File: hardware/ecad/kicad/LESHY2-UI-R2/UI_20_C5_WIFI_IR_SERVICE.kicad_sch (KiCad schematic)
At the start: 96 parts, among them J6 Samtec FTSH-105-01-L-DV-K-P-TR, J7 GCT RFPC-SMA32-FN-175-A, J8 Hirose U.FL-R-SMT-1(80), J9 GCT USB4105-GF-A, Q2 Diodes Incorporated 2N7002DW-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, Q3 Diodes Incorporated DMN2056U-7, Q4 Diodes Incorporated DMN2056U-7, Q5 Diodes Incorporated DMN2056U-7, SW18 Alps Alpine SKRTLAE010, SW19 Alps Alpine SKRTLAE010, U14 ESP32-C5-WROOM-1U-N8R8, U15 Texas Instruments TPD4E05U06D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, U16 KYOCERA AVX CP0603Q5425ENTR, U17 74LVC2G14GV,125, U18 SN74LVC1G74DCUR, U19 74HC20PW,118, U20 74LVC2G14GV,125, U21 Texas Instruments TPD2EUSB30A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, U22 onsemi FSUSB42MUX, U23 Vishay TSMP95000TT, U24 Vishay TSOP75238TR, U25 Texas Instruments TPS22919DCKR, U26 Nexperia 74LVC2G126DP,125, U27 SN74LVC1G08DCKR

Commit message: Bind H6 RF and USB routing geometry
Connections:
- net C5_SERVICE_USB_DM_BRANCH renamed C5_SERVICE_USB_BRANCH_N
- net C5_SERVICE_USB_DM_CONNECTOR renamed C5_SERVICE_USB_CONNECTOR_N
- net C5_SERVICE_USB_DP_BRANCH renamed C5_SERVICE_USB_BRANCH_P
- net C5_SERVICE_USB_DP_CONNECTOR renamed C5_SERVICE_USB_CONNECTOR_P
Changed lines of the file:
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@@
 		(effects (font (size 1.27 1.27)))
 	)
-	(label "C5_SERVICE_USB_DP_CONNECTOR"
+	(label "C5_SERVICE_USB_CONNECTOR_P"
 		(at 858.52 91.44 0)
 		(effects (font (size 1.27 1.27)))
 	)
-	(label "C5_SERVICE_USB_DM_CONNECTOR"
+	(label "C5_SERVICE_USB_CONNECTOR_N"
 		(at 858.52 93.98 0)
 		(effects (font (size 1.27 1.27)))
@@
 		(effects (font (size 1.27 1.27)) (justify right bottom))
 	)
-	(label "C5_SERVICE_USB_DP_CONNECTOR"
+	(label "C5_SERVICE_USB_CONNECTOR_P"
 		(at 899.16 88.90 180)
 		(effects (font (size 1.27 1.27)) (justify right bottom))
 	)
-	(label "C5_SERVICE_USB_DM_CONNECTOR"
+	(label "C5_SERVICE_USB_CONNECTOR_N"
 		(at 899.16 91.44 180)
 		(effects (font (size 1.27 1.27)) (justify right bottom))
@@
 		)
 	)
-	(label "C5_SERVICE_USB_DM_BRANCH"
+	(label "C5_SERVICE_USB_BRANCH_N"
 		(at 584.20 195.58 0)
 		(effects (font (size 1.27 1.27)))
 	)
-	(label "C5_SERVICE_USB_DM_CONNECTOR"
+	(label "C5_SERVICE_USB_CONNECTOR_N"
 		(at 624.84 195.58 180)
 		(effects (font (size 1.27 1.27)) (justify right bottom))
@@
 		)
 	)
-	(label "C5_SERVICE_USB_DP_BRANCH"
+	(label "C5_SERVICE_USB_BRANCH_P"
 		(at 858.52 205.74 0)
 		(effects (font (size 1.27 1.27)))
 	)
-	(label "C5_SERVICE_USB_DP_CONNECTOR"
+	(label "C5_SERVICE_USB_CONNECTOR_P"
 		(at 899.16 205.74 180)
 		(effects (font (size 1.27 1.27)) (justify right bottom))
@@
 		)
 	)
-	(label "C5_SERVICE_USB_DP_CONNECTOR"
+	(label "C5_SERVICE_USB_CONNECTOR_P"
 		(at 492.76 299.72 0)
 		(effects (font (size 1.27 1.27)))
 	)
-	(label "C5_SERVICE_USB_DM_CONNECTOR"
+	(label "C5_SERVICE_USB_CONNECTOR_N"
 		(at 492.76 302.26 0)
 		(effects (font (size 1.27 1.27)))
@@
 		(effects (font (size 1.27 1.27)))
 	)
-	(label "C5_SERVICE_USB_DM_BRANCH"
+	(label "C5_SERVICE_USB_BRANCH_N"
 		(at 716.28 297.18 180)
 		(effects (font (size 1.27 1.27)) (justify right bottom))
 	)
-	(label "C5_SERVICE_USB_DP_BRANCH"
+	(label "C5_SERVICE_USB_BRANCH_P"
 		(at 716.28 299.72 180)
 		(effects (font (size 1.27 1.27)) (justify right bottom))

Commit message: Canonicalize physical ground anchors
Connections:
- net /UI_10_S3_CORE_MEMORY_BOOT/POWER_GROUND is gone; now on net POWER_GROUND: U14.1 (GND), U14.28 (GND), U14.29 (GND), U14.30 (GND), U14.32 (GND)
- net C5_DBG_ESD_RETURN is gone; now on net POWER_GROUND: U15.3 (GND_3), U15.8 (GND_8)
- net C5_RF_GROUND is gone; now on net POWER_GROUND: J8.2 (SHELL), R94.2 (END_2)
- net C5_SMA_RF_GROUND is gone; now on net POWER_GROUND: J7.2 (GROUND_TOP_LEFT), J7.3 (GROUND_TOP_RIGHT), J7.4 (GROUND_BOTTOM_LEFT), J7.5 (GROUND_BOTTOM_RIGHT)
- net SAFETY_GROUND is gone; now on net POWER_GROUND: C21.2 (END_2), C23.2 (END_2), C24.2 (END_2), C25.2 (END_2), C26.2 (END_2), C27.2 (END_2), C31.2 (END_2), C32.2 (END_2), C37.2 (END_2), Q2.1 (S2), Q2.4 (S1), Q3.2 (S), Q4.2 (S), R111.2 (END_2), R123.2 (END_2), R125.2 (END_2), R127.2 (END_2), R85.2 (END_2), R87.2 (END_2), R89.2 (END_2), R91.2 (END_2), R92.2 (END_2), U17.2 (GND), U18.1 (CLK), U18.2 (D), U18.4 (GND), U19.7 (GND), U20.2 (GND), U27.3 (GND)
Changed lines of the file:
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@@
 		(effects (font (size 1.27 1.27)))
 	)
-	(hierarchical_label "SAFETY_GROUND"
+	(hierarchical_label "POWER_GROUND"
 		(shape bidirectional)
 		(at 76.20 50.80 180)
@@
 		(effects (font (size 1.27 1.27)))
 	)
-	(label "SAFETY_GROUND"
+	(label "POWER_GROUND"
 		(at 259.08 50.80 180)
 		(effects (font (size 1.27 1.27)) (justify right bottom))
@@
 		(effects (font (size 1.27 1.27)))
 	)
-	(label "SAFETY_GROUND"
+	(label "POWER_GROUND"
 		(at 350.52 50.80 180)
 		(effects (font (size 1.27 1.27)) (justify right bottom))
@@
 		(effects (font (size 1.27 1.27)))
 	)
-	(label "SAFETY_GROUND"
+	(label "POWER_GROUND"
 		(at 441.96 50.80 180)
 		(effects (font (size 1.27 1.27)) (justify right bottom))
@@
 		(effects (font (size 1.27 1.27)))
 	)
-	(label "SAFETY_GROUND"
+	(label "POWER_GROUND"
 		(at 533.40 50.80 180)
 		(effects (font (size 1.27 1.27)) (justify right bottom))
@@
 		(effects (font (size 1.27 1.27)))
 	)
-	(label "SAFETY_GROUND"
+	(label "POWER_GROUND"
 		(at 624.84 50.80 180)
 		(effects (font (size 1.27 1.27)) (justify right bottom))
@@
 		(effects (font (size 1.27 1.27)))
 	)
-	(hierarchical_label "POWER_GROUND"
-		(shape bidirectional)
+	(label "POWER_GROUND"
 		(at 716.28 50.80 180)
 		(effects (font (size 1.27 1.27)) (justify right bottom))
@@
 		(effects (font (size 1.27 1.27)))
 	)
-	(label "SAFETY_GROUND"
+	(label "POWER_GROUND"
 		(at 990.60 50.80 180)
 		(effects (font (size 1.27 1.27)) (justify right bottom))
@@
 		(effects (font (size 1.27 1.27)))
 	)
-	(label "SAFETY_GROUND"
+	(label "POWER_GROUND"
 		(at 1082.04 50.80 180)
 		(effects (font (size 1.27 1.27)) (justify right bottom))
@@
 		(effects (font (size 1.27 1.27)))
 	)
-	(label "SAFETY_GROUND"
+	(label "POWER_GROUND"
 		(at 441.96 86.36 180)
 		(effects (font (size 1.27 1.27)) (justify right bottom))
@@
 		(effects (font (size 1.27 1.27)))
 	)
-	(label "C5_SMA_RF_GROUND"
+	(label "POWER_GROUND"
 		(at 675.64 87.63 0)
 		(effects (font (size 1.27 1.27)))
 	)
-	(label "C5_SMA_RF_GROUND"
+	(label "POWER_GROUND"
 		(at 675.64 90.17 0)
 		(effects (font (size 1.27 1.27)))
 	)
-	(label "C5_SMA_RF_GROUND"
+	(label "POWER_GROUND"
 		(at 716.28 85.09 180)
 		(effects (font (size 1.27 1.27)) (justify right bottom))
 	)
-	(label "C5_SMA_RF_GROUND"
+	(label "POWER_GROUND"
 		(at 716.28 87.63 180)
 		(effects (font (size 1.27 1.27)) (justify right bottom))
@@
 		(effects (font (size 1.27 1.27)))
 	)
-	(label "C5_RF_GROUND"
+	(label "POWER_GROUND"
 		(at 807.72 86.36 180)
 		(effects (font (size 1.27 1.27)) (justify right bottom))
@@
 		)
 	)
-	(label "SAFETY_GROUND"
+	(label "POWER_GROUND"
 		(at 949.96 85.09 0)
 		(effects (font (size 1.27 1.27)))
@@
 		(effects (font (size 1.27 1.27)))
 	)
-	(label "SAFETY_GROUND"
+	(label "POWER_GROUND"
 		(at 990.60 85.09 180)
 		(effects (font (size 1.27 1.27)) (justify right bottom))
@@
 		(effects (font (size 1.27 1.27)))
 	)
-	(label "SAFETY_GROUND"
+	(label "POWER_GROUND"
 		(at 1041.40 88.90 0)
 		(effects (font (size 1.27 1.27)))
@@
 		(effects (font (size 1.27 1.27)))
 	)
-	(label "SAFETY_GROUND"
+	(label "POWER_GROUND"
 		(at 35.56 124.46 0)
 		(effects (font (size 1.27 1.27)))
@@
 		(effects (font (size 1.27 1.27)))
 	)
-	(label "SAFETY_GROUND"
+	(label "POWER_GROUND"
 		(at 899.16 134.62 180)
 		(effects (font (size 1.27 1.27)) (justify right bottom))
@@
 		(effects (font (size 1.27 1.27)))
 	)
-	(label "SAFETY_GROUND"
+	(label "POWER_GROUND"
 		(at 167.64 157.48 180)
 		(effects (font (size 1.27 1.27)) (justify right bottom))
@@
 		(effects (font (size 1.27 1.27)))
 	)
-	(label "SAFETY_GROUND"
+	(label "POWER_GROUND"
 		(at 350.52 157.48 180)
 		(effects (font (size 1.27 1.27)) (justify right bottom))
@@
 		(effects (font (size 1.27 1.27)))
 	)
-	(label "SAFETY_GROUND"
+	(label "POWER_GROUND"
 		(at 533.40 157.48 180)
 		(effects (font (size 1.27 1.27)) (justify right bottom))
@@
 		(effects (font (size 1.27 1.27)))
 	)
-	(label "SAFETY_GROUND"
+	(label "POWER_GROUND"
 		(at 716.28 157.48 180)
 		(effects (font (size 1.27 1.27)) (justify right bottom))
@@
 		(effects (font (size 1.27 1.27)))
 	)
-	(label "C5_RF_GROUND"
+	(label "POWER_GROUND"
 		(at 990.60 157.48 180)
 		(effects (font (size 1.27 1.27)) (justify right bottom))
@@
 		(effects (font (size 1.27 1.27)))
 	)
-	(label "SAFETY_GROUND"
+	(label "POWER_GROUND"
 		(at 167.64 228.60 180)
 		(effects (font (size 1.27 1.27)) (justify right bottom))
@@
 		(effects (font (size 1.27 1.27)))
 	)
-	(label "SAFETY_GROUND"
+	(label "POWER_GROUND"
 		(at 167.64 264.16 180)
 		(effects (font (size 1.27 1.27)) (justify right bottom))
@@
 		(effects (font (size 1.27 1.27)))
 	)
-	(label "SAFETY_GROUND"
+	(label "POWER_GROUND"
 		(at 350.52 264.16 180)
 		(effects (font (size 1.27 1.27)) (justify right bottom))
@@
 		(effects (font (size 1.27 1.27)))
 	)
-	(label "SAFETY_GROUND"
+	(label "POWER_GROUND"
 		(at 533.40 264.16 180)
 		(effects (font (size 1.27 1.27)) (justify right bottom))
@@
 		)
 	)
-	(hierarchical_label "/UI_10_S3_CORE_MEMORY_BOOT/POWER_GROUND"
-		(shape bidirectional)
+	(label "POWER_GROUND"
 		(at 584.20 264.16 0)
 		(effects (font (size 1.27 1.27)))
@@
 	(no_connect (at 624.84 289.56)
 	)
-	(label "/UI_10_S3_CORE_MEMORY_BOOT/POWER_GROUND"
+	(label "POWER_GROUND"
 		(at 624.84 292.10 180)
 		(effects (font (size 1.27 1.27)) (justify right bottom))
 	)
-	(label "/UI_10_S3_CORE_MEMORY_BOOT/POWER_GROUND"
+	(label "POWER_GROUND"
 		(at 624.84 294.64 180)
 		(effects (font (size 1.27 1.27)) (justify right bottom))
 	)
-	(label "/UI_10_S3_CORE_MEMORY_BOOT/POWER_GROUND"
+	(label "POWER_GROUND"
 		(at 624.84 297.18 180)
 		(effects (font (size 1.27 1.27)) (justify right bottom))
@@
 	(no_connect (at 624.84 299.72)
 	)
-	(label "/UI_10_S3_CORE_MEMORY_BOOT/POWER_GROUND"
+	(label "POWER_GROUND"
 		(at 624.84 302.26 180)
 		(effects (font (size 1.27 1.27)) (justify right bottom))
@@
 		(effects (font (size 1.27 1.27)))
 	)
-	(label "C5_DBG_ESD_RETURN"
+	(label "POWER_GROUND"
 		(at 858.52 279.40 0)
 		(effects (font (size 1.27 1.27)))
@@
 	(no_connect (at 899.16 276.86)
 	)
-	(label "C5_DBG_ESD_RETURN"
+	(label "POWER_GROUND"
 		(at 899.16 279.40 180)
 		(effects (font (size 1.27 1.27)) (justify right bottom))
@@
 		(effects (font (size 1.27 1.27)))
 	)
-	(label "SAFETY_GROUND"
+	(label "POWER_GROUND"
 		(at 127.00 300.99 0)
 		(effects (font (size 1.27 1.27)))
@@
 		)
 	)
-	(label "SAFETY_GROUND"
+	(label "POWER_GROUND"
 		(at 218.44 297.18 0)
 		(effects (font (size 1.27 1.27)))
 	)
-	(label "SAFETY_GROUND"
+	(label "POWER_GROUND"
 		(at 218.44 299.72 0)
 		(effects (font (size 1.27 1.27)))
@@
 	(no_connect (at 218.44 302.26)
 	)
-	(label "SAFETY_GROUND"
+	(label "POWER_GROUND"
 		(at 218.44 304.80 0)
 		(effects (font (size 1.27 1.27)))
@@
 		(effects (font (size 1.27 1.27)))
 	)
-	(label "SAFETY_GROUND"
+	(label "POWER_GROUND"
 		(at 309.88 312.42 0)
 		(effects (font (size 1.27 1.27)))
@@
 		(effects (font (size 1.27 1.27)))
 	)
-	(label "SAFETY_GROUND"
+	(label "POWER_GROUND"
 		(at 401.32 300.99 0)
 		(effects (font (size 1.27 1.27)))
@@
 		(effects (font (size 1.27 1.27)))
 	)
-	(label "SAFETY_GROUND"
+	(label "POWER_GROUND"
 		(at 584.20 336.55 0)
 		(effects (font (size 1.27 1.27)))

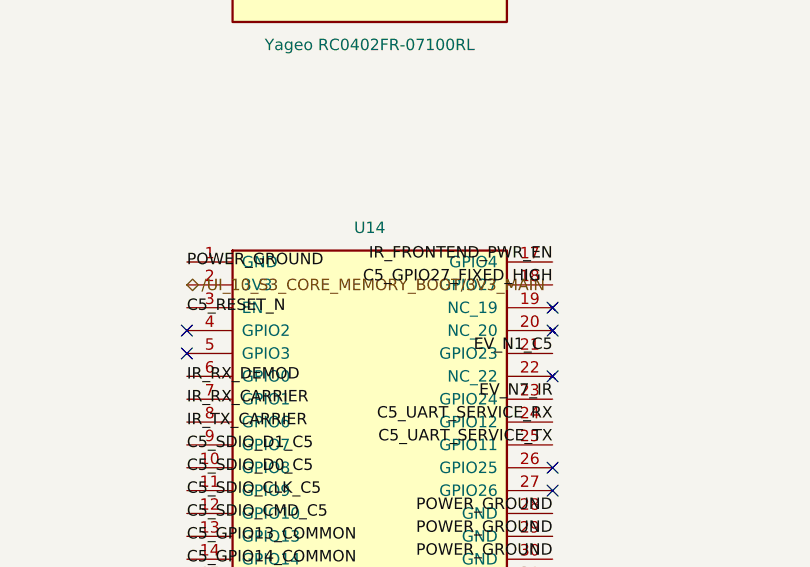
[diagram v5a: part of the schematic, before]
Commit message: Correct SMA geometry and module power; bind verification to current boards
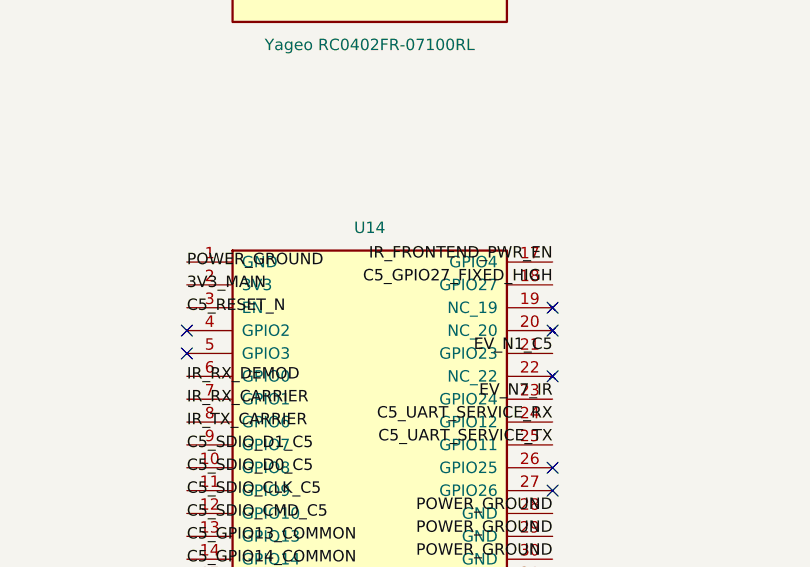
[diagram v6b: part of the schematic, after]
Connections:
- net /UI_10_S3_CORE_MEMORY_BOOT/3V3_MAIN is gone; now on net 3V3_MAIN: U14.2 (3V3)
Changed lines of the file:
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@@
 		(effects (font (size 1.27 1.27)))
 	)
-	(hierarchical_label "/UI_10_S3_CORE_MEMORY_BOOT/3V3_MAIN"
-		(shape bidirectional)
+	(label "3V3_MAIN"
 		(at 584.20 266.70 0)
 		(effects (font (size 1.27 1.27)))

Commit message: Correct exact connector and protection geometry; expand electrical review
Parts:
- U21: footprint Package_TO_SOT_SMD:SOT-23 -> Package_TO_SOT_SMD:Texas_DRT-3
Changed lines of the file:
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@@
 			(effects (font (size 1.27 1.27)))
 		)
-		(property "Footprint" "Package_TO_SOT_SMD:SOT-23"
+		(property "Footprint" "Package_TO_SOT_SMD:Texas_DRT-3"
 			(at 513.08 300.99 0)
 			(show_name no)

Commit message: Correct exact RF lands and reopen native power prerequisites
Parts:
- U16: footprint Leshy2:CP0603Q5425ENTR -> Leshy2_R2:CP0603Q5425ENTR
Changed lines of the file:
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@@
 			(effects (font (size 1.27 1.27)))
 		)
-		(property "Footprint" "Leshy2:CP0603Q5425ENTR"
+		(property "Footprint" "Leshy2_R2:CP0603Q5425ENTR"
 			(at 55.88 300.99 0)
 			(show_name no)
